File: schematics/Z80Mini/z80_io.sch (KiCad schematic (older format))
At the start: 24 parts, among them J3 USB_B_Micro, J4 Conn_02x10_Counter_Clockwise, SW2 SW_DIP_x04, U7 82C55A, U8 16550, U9 FT232RL

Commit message: Latest modifications and update to v1.1 and first successifully VDP routines test.
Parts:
- removed C13, C14, C16: 0.1, Capacitor_THT:C_Disc_D3.0mm_W1.6mm_P2.50mm, symbol Device:C
- removed C15: 10uF, Capacitor_THT:CP_Radial_D5.0mm_P2.00mm, symbol Device:CP1
- added C14: 10uF, Capacitor_THT:CP_Radial_D5.0mm_P2.00mm, symbol Device:CP
- added C15, C17: 100nF, Capacitor_THT:C_Disc_D7.0mm_W2.5mm_P5.00mm, symbol Device:C
- added C20, C4: 0.1uF, Capacitor_THT:C_Disc_D3.0mm_W1.6mm_P2.50mm, symbol Device:C
- added JP3: USB_POWER, Connector_PinHeader_2.00mm:PinHeader_1x02_P2.00mm_Vertical, symbol Device:Jumper_NO_Small
- added JP4: SELF_POWER, Connector_PinHeader_2.00mm:PinHeader_1x03_P2.00mm_Vertical, symbol Device:Jumper_NC_Dual
- added Q2: IRLML6402, Package_TO_SOT_SMD:SOT-23, symbol Transistor_FET:IRLML6402
- added R18: 1K, Resistor_THT:R_Axial_DIN0207_L6.3mm_D2.5mm_P7.62mm_Horizontal, symbol Device:R
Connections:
- wire segments 211 -> 228
- no-connect marks 16 -> 14
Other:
- moved on the sheet: FB1

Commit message: Added new code for core written in C with Z88DK
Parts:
- C14: footprint Capacitor_THT:CP_Radial_D5.0mm_P2.00mm -> Capacitor_THT:CP_Radial_D5.0mm_P2.50mm
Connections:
- net labels added: DSR, DTR, RX, TX
- wire segments 228 -> 231
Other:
- moved on the sheet: C20, C4, JP4, Q2, R18
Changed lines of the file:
@@
 	7350 3850 7350 2100
 Wire Wire Line
-	7350 2100 10100 2100
+	7350 2100 7800 2100
 Wire Wire Line
 	10100 2100 10100 3050
@@
 	7450 3950 7450 2200
 Wire Wire Line
-	7450 2200 10200 2200
+	7450 2200 7900 2200
 Wire Wire Line
 	10200 2200 10200 3150
@@
 	10450 3250 9850 3250
 Wire Wire Line
-	6850 2650 7050 2650
-Wire Wire Line
-	7050 2650 7050 2550
-Wire Wire Line
-	7050 1800 10550 1800
+	6850 2650 6950 2650
 Wire Wire Line
 	10550 1800 10550 3450
@@
 	6850 3150 7550 3150
 Wire Wire Line
-	7550 3150 7550 2300
-Wire Wire Line
-	7550 2300 10000 2300
-Wire Wire Line
-	10000 2300 10000 3550
-Wire Wire Line
 	10000 3550 9850 3550
 NoConn ~ 9850 4450
@@
 Wire Wire Line
 	10000 3650 10000 3550
-Connection ~ 10000 3550
 NoConn ~ 9850 3750
-Wire Wire Line
-	6850 2550 7050 2550
-Connection ~ 7050 2550
-Wire Wire Line
-	7050 2550 7050 1800
 Wire Wire Line
 	7900 3350 7900 5150
@@
 Text GLabel 4700 4750 0    50   Input ~ 0
 RD
-Wire Wire Line
-	6850 2450 6950 2450
-Wire Wire Line
-	6950 2450 6950 1650
 Text Label 650  1200 0    50   ~ 0
 A[0..15]
@@
 Wire Bus Line
 	4050 1200 4150 1200
-Wire Wire Line
-	5850 1650 6950 1650
 Text Label 1250 5700 0    50   ~ 0
 D[0..7]
@@
 F 0 "C14" H 7915 2796 50  0000 L CNN
 F 1 "10uF" H 7915 2705 50  0000 L CNN
-F 2 "Capacitor_THT:CP_Radial_D5.0mm_P2.00mm" H 7838 2600 50  0001 C CNN
+F 2 "Capacitor_THT:CP_Radial_D5.0mm_P2.50mm" H 7838 2600 50  0001 C CNN
 F 3 "~" H 7800 2750 50  0001 C CNN
 	1    7800 2750
@@
 Wire Wire Line
 	8950 2500 9150 2500
-Connection ~ 9150 2500
 Wire Wire Line
 	9150 2500 9150 2750
@@
 L Transistor_FET:IRLML6402 Q2
 U 1 1 5E9FA872
-P 10550 4350
-F 0 "Q2" H 10756 4396 50  0000 L CNN
-F 1 "IRLML6402" H 10756 4305 50  0000 L CNN
-F 2 "Package_TO_SOT_SMD:SOT-23" H 10750 4275 50  0001 L CIN
-F 3 "https://www.infineon.com/dgdl/irlml6402pbf.pdf?fileId=5546d462533600a401535668d5c2263c" H 10550 4350 50  0001 L CNN
-	1    10550 4350
-	1    0    0    -1
+P 10650 1100
+F 0 "Q2" H 10856 1146 50  0000 L CNN
+F 1 "IRLML6402" H 10856 1055 50  0000 L CNN
+F 2 "Package_TO_SOT_SMD:SOT-23" H 10850 1025 50  0001 L CIN
+F 3 "https://www.infineon.com/dgdl/irlml6402pbf.pdf?fileId=5546d462533600a401535668d5c2263c" H 10650 1100 50  0001 L CNN
+	1    10650 1100
+	0    -1   -1   0
 $EndComp
 $Comp
 L Device:R R18
 U 1 1 5EA0C7A8
-P 10100 4350
-F 0 "R18" H 10030 4304 50  0000 R CNN
-F 1 "1K" H 10030 4395 50  0000 R CNN
-F 2 "Resistor_THT:R_Axial_DIN0207_L6.3mm_D2.5mm_P7.62mm_Horizontal" V 10030 4350 50  0001 C CNN
-F 3 "~" H 10100 4350 50  0001 C CNN
-	1    10100 4350
-	0    -1   -1   0
-$EndComp
-Wire Wire Line
-	9850 4350 9950 4350
-Wire Wire Line
-	10250 4350 10350 4350
+P 10650 1550
+F 0 "R18" H 10580 1504 50  0000 R CNN
+F 1 "1K" H 10580 1595 50  0000 R CNN
+F 2 "Resistor_THT:R_Axial_DIN0207_L6.3mm_D2.5mm_P7.62mm_Horizontal" V 10580 1550 50  0001 C CNN
+F 3 "~" H 10650 1550 50  0001 C CNN
+	1    10650 1550
+	-1   0    0    1
+$EndComp
+Wire Wire Line
+	10650 1400 10650 1300
 $Comp
 L Device:C C4
 U 1 1 5EA2C632
-P 10400 4100
-F 0 "C4" H 10515 4146 50  0000 L CNN
-F 1 "0.1uF" H 10515 4055 50  0000 L CNN
-F 2 "Capacitor_THT:C_Disc_D3.0mm_W1.6mm_P2.50mm" H 10438 3950 50  0001 C CNN
-F 3 "~" H 10400 4100 50  0001 C CNN
-	1    10400 4100
-	0    -1   -1   0
-$EndComp
-Wire Wire Line
-	10250 4100 10250 4350
-Connection ~ 10250 4350
-Wire Wire Line
-	10550 4100 10650 4100
-Wire Wire Line
-	10650 4100 10650 4150
+P 10400 1250
+F 0 "C4" H 10515 1296 50  0000 L CNN
+F 1 "0.1uF" H 10515 1205 50  0000 L CNN
+F 2 "Capacitor_THT:C_Disc_D3.0mm_W1.6mm_P2.50mm" H 10438 1100 50  0001 C CNN
+F 3 "~" H 10400 1250 50  0001 C CNN
+	1    10400 1250
+	-1   0    0    1
+$EndComp
+Wire Wire Line
+	10400 1400 10650 1400
+Connection ~ 10650 1400
+Wire Wire Line
+	10400 1100 10400 1000
+Wire Wire Line
+	10400 1000 10450 1000
 $Comp
 L Device:C C20
 U 1 1 5EA4B1DC
-P 10400 3750
-F 0 "C20" H 10515 3796 50  0000 L CNN
-F 1 "0.1uF" H 10515 3705 50  0000 L CNN
-F 2 "Capacitor_THT:C_Disc_D3.0mm_W1.6mm_P2.50mm" H 10438 3600 50  0001 C CNN
-F 3 "~" H 10400 3750 50  0001 C CNN
-	1    10400 3750
-	0    -1   -1   0
-$EndComp
-Wire Wire Line
-	10550 3750 10650 3750
-Wire Wire Line
-	10650 3750 10650 4100
-Connection ~ 10650 4100
-Wire Wire Line
-	9150 2500 11000 2500
-Wire Wire Line
-	11000 2500 11000 4650
-Wire Wire Line
-	11000 4650 10650 4650
-Wire Wire Line
-	10650 4650 10650 4550
+P 10050 1250
+F 0 "C20" H 10165 1296 50  0000 L CNN
+F 1 "0.1uF" H 10165 1205 50  0000 L CNN
+F 2 "Capacitor_THT:C_Disc_D3.0mm_W1.6mm_P2.50mm" H 10088 1100 50  0001 C CNN
+F 3 "~" H 10050 1250 50  0001 C CNN
+	1    10050 1250
+	-1   0    0    1
+$EndComp
+Wire Wire Line
+	10050 1100 10050 1000
+Wire Wire Line
+	10050 1000 10400 1000
+Connection ~ 10400 1000
 $Comp
 L power:GND #PWR0102
 U 1 1 5EA6BF43
-P 10150 3800
-F 0 "#PWR0102" H 10150 3550 50  0001 C CNN
-F 1 "GND" H 10155 3627 50  0000 C CNN
-F 2 "" H 10150 3800 50  0001 C CNN
-F 3 "" H 10150 3800 50  0001 C CNN
-	1    10150 3800
-	1    0    0    -1
-$EndComp
-Wire Wire Line
-	10150 3750 10250 3750
-Wire Wire Line
-	10150 3750 10150 3800
+P 10050 1450
+F 0 "#PWR0102" H 10050 1200 50  0001 C CNN
+F 1 "GND" H 10055 1277 50  0000 C CNN
+F 2 "" H 10050 1450 50  0001 C CNN
+F 3 "" H 10050 1450 50  0001 C CNN
+	1    10050 1450
+	1    0    0    -1
+$EndComp
+Wire Wire Line
+	10050 1400 10050 1450
 $Comp
 L Device:Jumper_NO_Small JP3
@@
 L power:VCC #PWR0103
 U 1 1 5EAC606A
-P 9450 1050
-F 0 "#PWR0103" H 9450 900 50  0001 C CNN
-F 1 "VCC" H 9450 1200 50  0000 C CNN
-F 2 "" H 9450 1050 50  0001 C CNN
-F 3 "" H 9450 1050 50  0001 C CNN
-	1    9450 1050
+P 9450 850
+F 0 "#PWR0103" H 9450 700 50  0001 C CNN
+F 1 "VCC" H 9450 1000 50  0000 C CNN
+F 2 "" H 9450 850 50  0001 C CNN
+F 3 "" H 9450 850 50  0001 C CNN
+	1    9450 850
 	1    0    0    -1
 $EndComp
@@
 L Device:Jumper_NC_Dual JP4
 U 1 1 5EAC6911
-P 9450 1200
-F 0 "JP4" H 9450 1347 50  0000 C CNN
-F 1 "SELF_POWER" H 9450 1438 50  0000 C CNN
-F 2 "Connector_PinHeader_2.00mm:PinHeader_1x03_P2.00mm_Vertical" H 9450 1200 50  0001 C CNN
-F 3 "~" H 9450 1200 50  0001 C CNN
-	1    9450 1200
+P 9450 1000
+F 0 "JP4" H 9450 1147 50  0000 C CNN
+F 1 "SELF_POWER" H 9450 1238 50  0000 C CNN
+F 2 "Connector_PinHeader_2.00mm:PinHeader_1x03_P2.00mm_Vertical" H 9450 1000 50  0001 C CNN
+F 3 "~" H 9450 1000 50  0001 C CNN
+	1    9450 1000
 	-1   0    0    1
 $EndComp
 Wire Wire Line
-	9450 1100 9450 1050
-Wire Wire Line
-	9150 1200 9200 1200
-Wire Wire Line
-	9150 1200 9150 2500
-Wire Wire Line
-	10650 3750 10650 1200
-Wire Wire Line
-	10650 1200 9700 1200
-Connection ~ 10650 3750
+	9450 900  9450 850
 Wire Wire Line
 	7700 2500 7700 4850
@@
 	7500 4200 7500 4150
 Connection ~ 7500 4200
+Wire Wire Line
+	6850 2450 6850 1650
+Wire Wire Line
+	6850 1650 5850 1650
+Wire Wire Line
+	6950 2650 6950 2550
+Wire Wire Line
+	7800 2100 7800 1250
+Connection ~ 7800 2100
+Wire Wire Line
+	7800 2100 10100 2100
+Wire Wire Line
+	7900 2200 7900 1250
+Connection ~ 7900 2200
+Wire Wire Line
+	7900 2200 10200 2200
+Text HLabel 6950 1250 1    50   Output ~ 0
+DSR
+Text HLabel 7550 1250 1    50   Output ~ 0
+DTR
+Text HLabel 7800 1250 1    50   Output ~ 0
+RX
+Text HLabel 7900 1250 1    50   Output ~ 0
+TX
+Connection ~ 6950 2550
+Wire Wire Line
+	6950 2550 6950 1800
+Wire Wire Line
+	6950 2550 6850 2550
+Wire Wire Line
+	6950 1800 10550 1800
+Connection ~ 6950 1800
+Wire Wire Line
+	6950 1800 6950 1250
+Wire Wire Line
+	9700 1000 10050 1000
+Connection ~ 10050 1000
+Wire Wire Line
+	10850 1000 11000 1000
+Wire Wire Line
+	9850 4350 10650 4350
+Connection ~ 10000 3550
+Wire Wire Line
+	10000 2300 10000 3550
+Wire Wire Line
+	7550 3150 7550 2300
+Wire Wire Line
+	7550 2300 7550 1250
+Connection ~ 7550 2300
+Wire Wire Line
+	7550 2300 10000 2300
+Wire Wire Line
+	10650 1700 10650 4350
+Wire Wire Line
+	9150 2500 11000 2500
+Wire Wire Line
+	11000 1000 11000 2500
+Connection ~ 9150 2500
+Wire Wire Line
+	8950 1000 8950 2500
+Wire Wire Line
+	8950 1000 9200 1000
 Wire Bus Line
 	650  1200 650  3100

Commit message: Latest changes on vdp routines and bas32k added new COLOR instruction
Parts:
- JP3: footprint Connector_PinHeader_2.00mm:PinHeader_1x02_P2.00mm_Vertical -> Connector_PinHeader_2.54mm:PinHeader_1x02_P2.54mm_Vertical
- JP4: footprint Connector_PinHeader_2.00mm:PinHeader_1x03_P2.00mm_Vertical -> Connector_PinHeader_2.54mm:PinHeader_1x03_P2.54mm_Vertical
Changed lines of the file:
@@
 F 0 "JP3" V 7654 4998 50  0000 L CNN
 F 1 "USB_POWER" V 7745 4998 50  0000 L CNN
-F 2 "Connector_PinHeader_2.00mm:PinHeader_1x02_P2.00mm_Vertical" H 7700 4950 50  0001 C CNN
+F 2 "Connector_PinHeader_2.54mm:PinHeader_1x02_P2.54mm_Vertical" H 7700 4950 50  0001 C CNN
 F 3 "~" H 7700 4950 50  0001 C CNN
 	1    7700 4950
@@
 F 0 "JP4" H 9450 1147 50  0000 C CNN
 F 1 "SELF_POWER" H 9450 1238 50  0000 C CNN
-F 2 "Connector_PinHeader_2.00mm:PinHeader_1x03_P2.00mm_Vertical" H 9450 1000 50  0001 C CNN
+F 2 "Connector_PinHeader_2.54mm:PinHeader_1x03_P2.54mm_Vertical" H 9450 1000 50  0001 C CNN
 F 3 "~" H 9450 1000 50  0001 C CNN
 	1    9450 1000

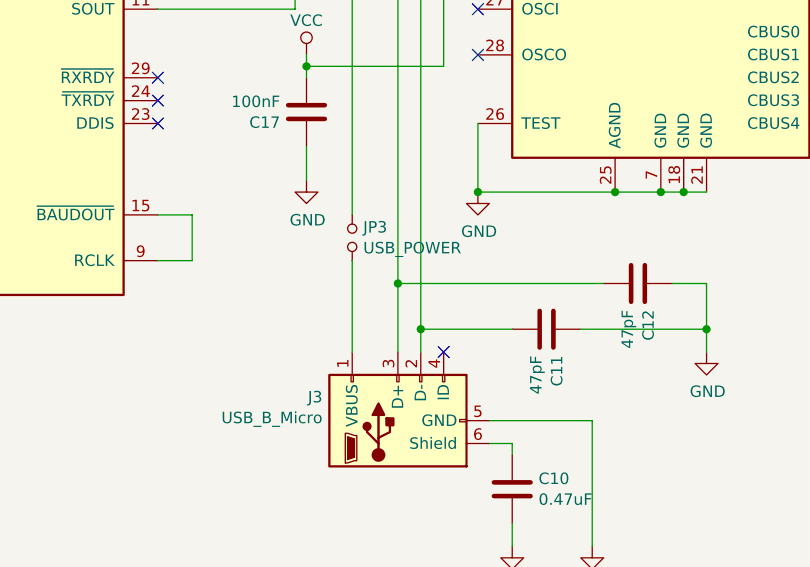
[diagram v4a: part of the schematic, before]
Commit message: Created new schematic for TTLSerial to USB, I2C and RS232
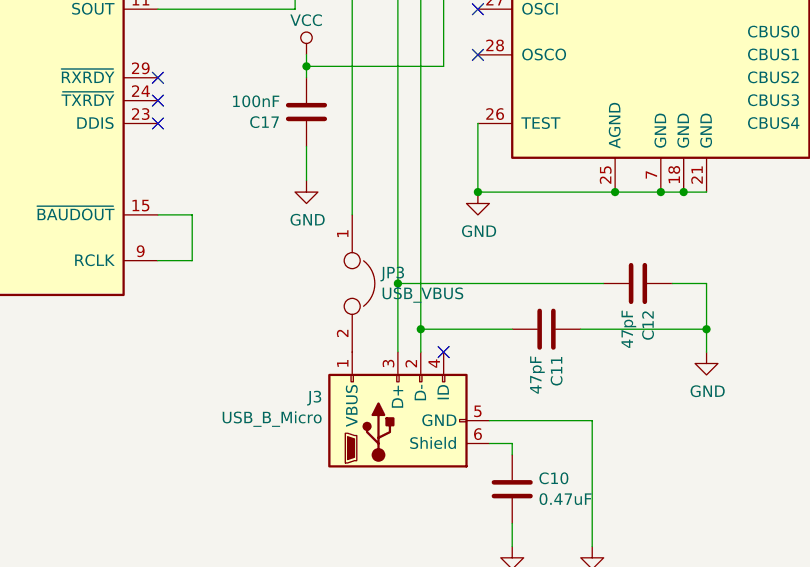
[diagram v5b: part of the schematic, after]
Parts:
- removed JP3: USB_POWER, Connector_PinHeader_2.54mm:PinHeader_1x02_P2.54mm_Vertical, symbol Device:Jumper_NO_Small
- added JP3: USB_VBUS, Connector_PinHeader_2.54mm:PinHeader_1x02_P2.54mm_Vertical, symbol Device:Jumper
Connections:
- wire segments 231 -> 230
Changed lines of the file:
@@
 EESchema Schematic File Version 4
-LIBS:Z80Mini-cache
 EELAYER 30 0
 EELAYER END
@@
 	10050 1400 10050 1450
 $Comp
-L Device:Jumper_NO_Small JP3
-U 1 1 5EABC98E
-P 7700 4950
-F 0 "JP3" V 7654 4998 50  0000 L CNN
-F 1 "USB_POWER" V 7745 4998 50  0000 L CNN
-F 2 "Connector_PinHeader_2.54mm:PinHeader_1x02_P2.54mm_Vertical" H 7700 4950 50  0001 C CNN
-F 3 "~" H 7700 4950 50  0001 C CNN
-	1    7700 4950
-	0    1    1    0
-$EndComp
-Wire Wire Line
-	7700 5050 7700 5450
-$Comp
 L power:VCC #PWR0103
 U 1 1 5EAC606A
@@
 Wire Wire Line
 	9450 900  9450 850
-Wire Wire Line
-	7700 2500 7700 4850
 $Comp
 L power:VCC #PWR0132
@@
 Connection ~ 9150 2500
 Wire Wire Line
+	8950 1000 9200 1000
+Wire Wire Line
+	7700 2500 7700 4850
+Wire Wire Line
 	8950 1000 8950 2500
-Wire Wire Line
-	8950 1000 9200 1000
+$Comp
+L Device:Jumper JP3
+U 1 1 5F4EAF1C
+P 7700 5150
+F 0 "JP3" V 7654 5277 50  0000 L CNN
+F 1 "USB_VBUS" V 7745 5277 50  0000 L CNN
+F 2 "Connector_PinHeader_2.54mm:PinHeader_1x02_P2.54mm_Vertical" H 7700 5150 50  0001 C CNN
+F 3 "~" H 7700 5150 50  0001 C CNN
+	1    7700 5150
+	0    1    1    0
+$EndComp
 Wire Bus Line
 	650  1200 650  3100
